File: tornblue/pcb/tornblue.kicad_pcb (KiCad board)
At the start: 2 copper layers, 140.7 x 102.9 mm, 78 parts, among them J1 BATT, J2 SWD, J3 BREAKOUT, J4 USB C - USB2.0, Q1 AO3401A, Q2 AO3401A, SW1 SW_Push, SW10 SW_Push, SW11 SW_Push, SW12 SW_Push, SW13 SW_Push, SW14 SW_Push, SW15 SW_Push, SW16 SW_Push, SW17 SW_Push, SW18 SW_Push, SW19 EC11, SW2 SW_Push, SW20 SW_Push, SW21 SW_Push, SW22 EC11, SW23 RESET, SW3 SW_Push, SW4 SW_Push, SW5 SW_Push, SW6 SW_Push, SW7 SW_Push, SW8 SW_Push, SW9 SW_Push, U1 XC6220, U2 TP4056, U3 nRF52840_holyiot_18010, U4 SRV05-4

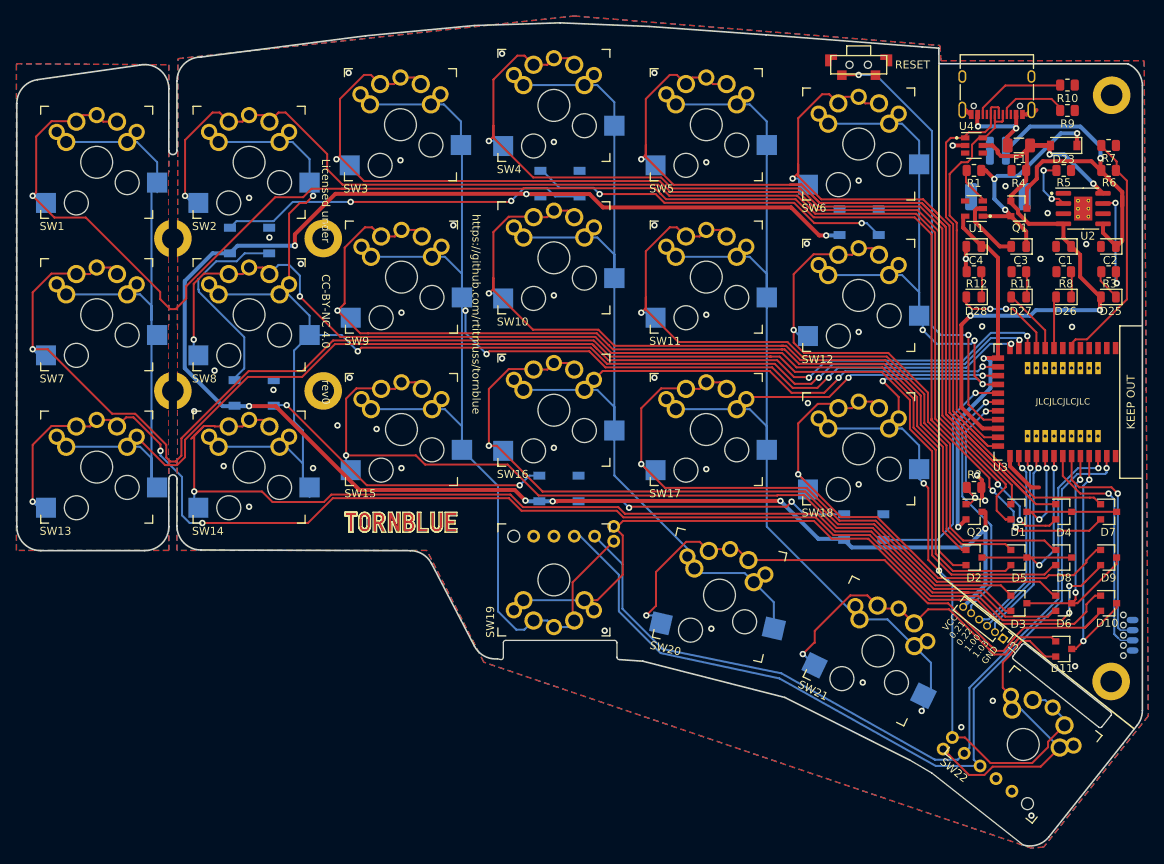
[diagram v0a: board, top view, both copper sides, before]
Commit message: Use m3 mounting holes
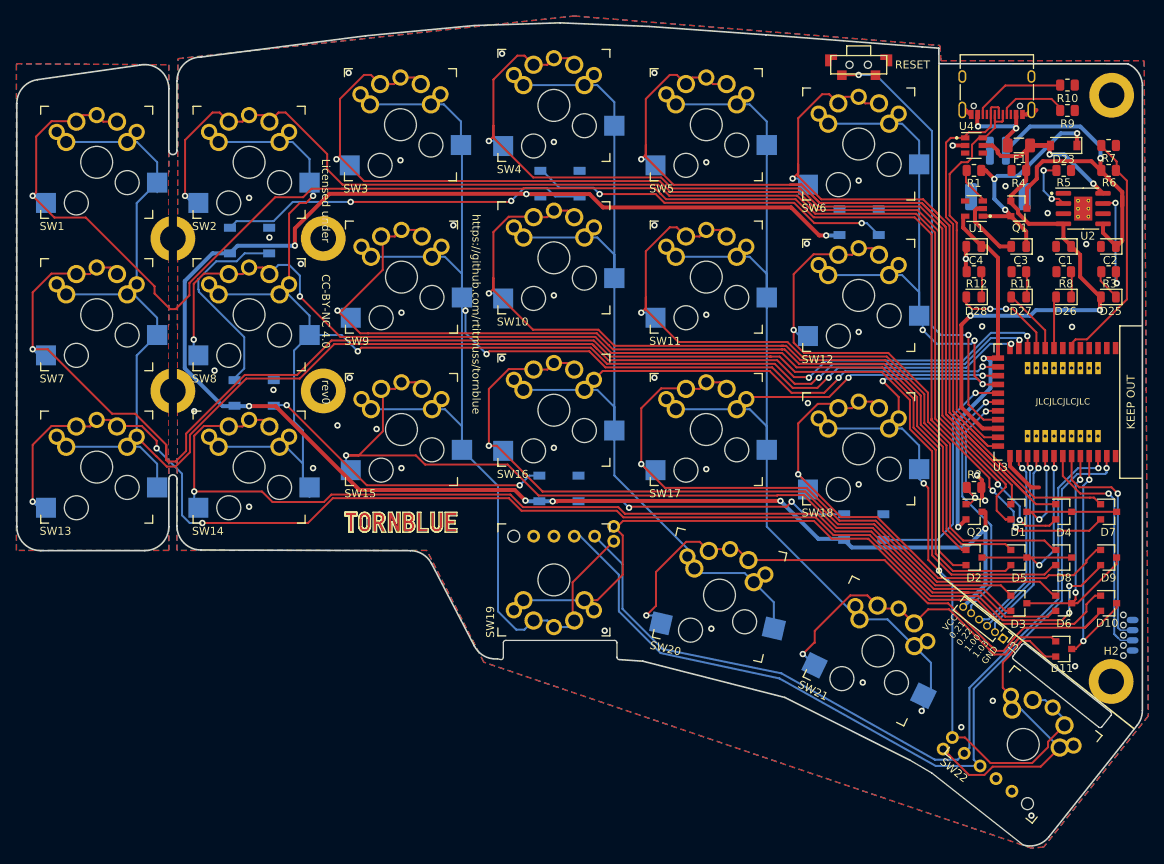
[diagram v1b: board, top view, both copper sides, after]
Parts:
- H1, H2, H3, H4: footprint MountingHole:MountingHole_2.7mm_M2.5_DIN965_Pad -> MountingHole:MountingHole_3.2mm_M3_DIN965_Pad
- H5, H6: footprint tornblue:MountingHole_2.7mm_M2.5_DIN965_Pad_Slot -> tornblue:MountingHole_3.2mm_M3_DIN965_Pad_Slot
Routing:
- net COL0: track 222.2 -> 212.7 mm
- net Net-(D2-Pad2): track 123.8 -> 121.5 mm
- net Net-(D6-Pad2): track 138.4 -> 136.1 mm
- net Net-(D8-Pad2): track 185.7 -> 187.8 mm
- net Net-(D9-Pad2): track 166.3 -> 165.4 mm
- net Net-(D3-Pad2): track 111.4 -> 110.6 mm
- net GND: vias 50 -> 49

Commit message: Smooth board outline
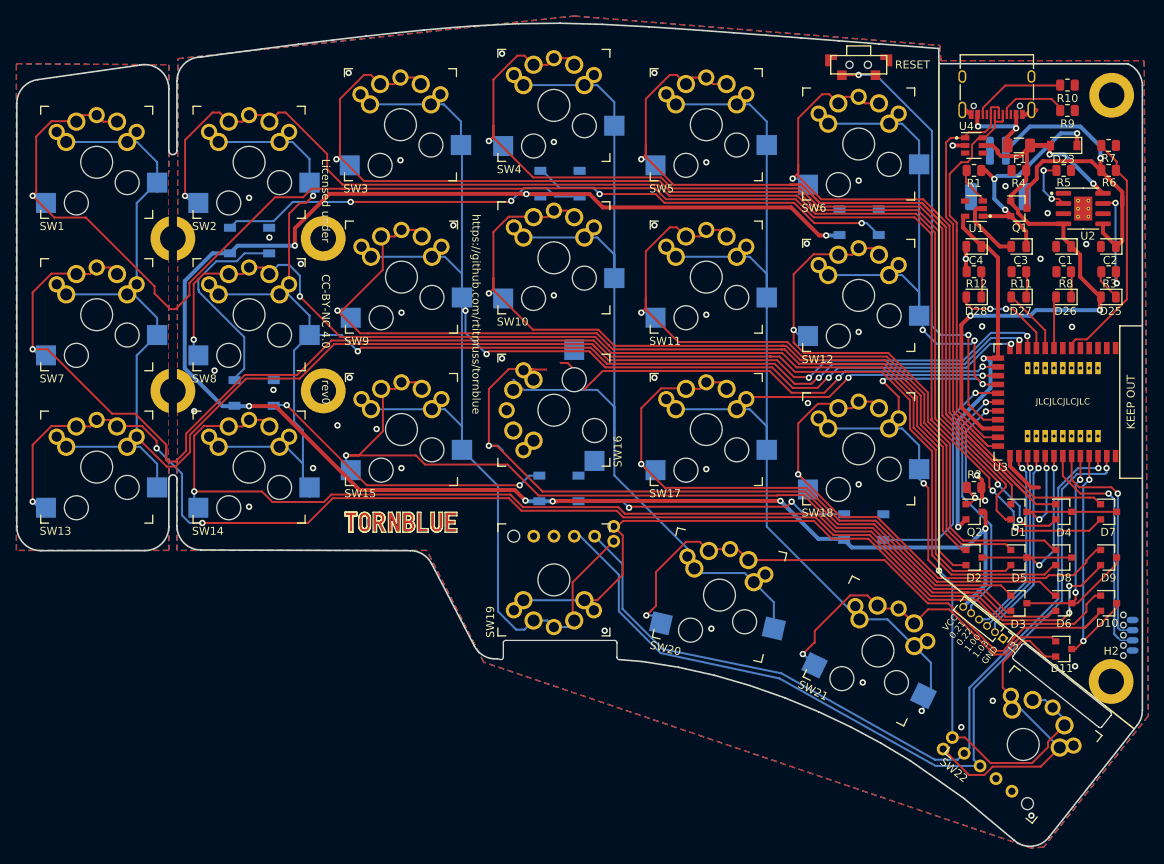
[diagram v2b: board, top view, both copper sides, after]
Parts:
- turned SW16 to 90 degrees
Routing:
- net GND: vias 49 -> 48
- net (no net): vias 0 -> 1
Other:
- outline, holes or cut-outs redrawn

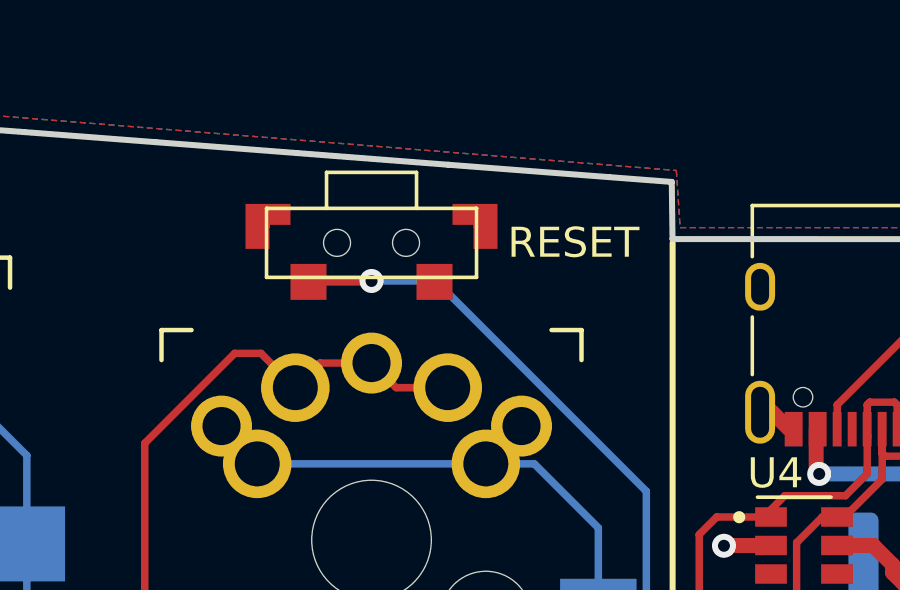
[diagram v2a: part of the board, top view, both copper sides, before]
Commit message: Change to lower profile reset switch
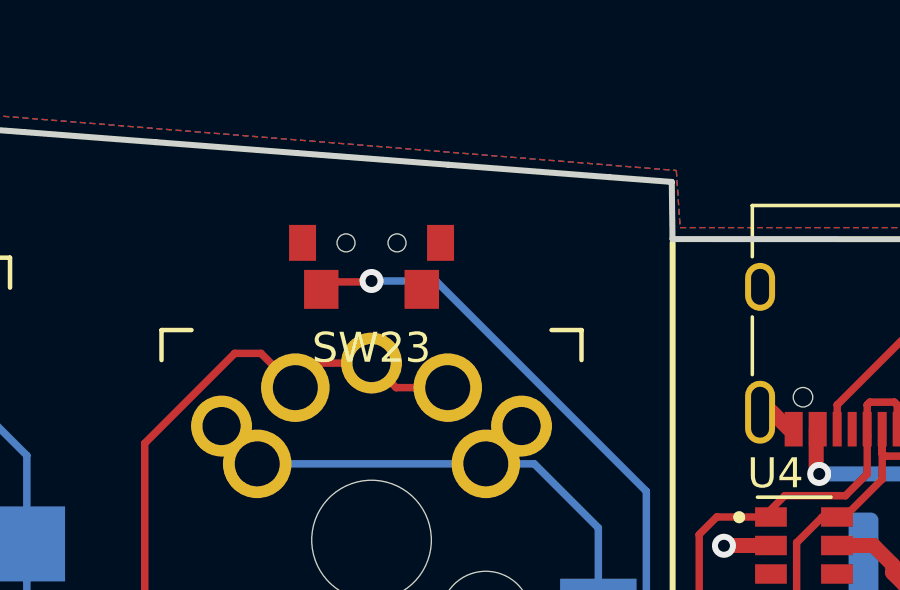
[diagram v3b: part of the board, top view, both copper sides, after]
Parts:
- SW23: footprint tornblue:SW_SPST_TS-1012E-26 -> tornblue:SW_SPST_TS24CA
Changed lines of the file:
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@@
   (layers
     (0 F.Cu signal)
-    (31 B.Cu signal hide)
+    (31 B.Cu signal)
     (32 B.Adhes user hide)
     (33 F.Adhes user hide)
@@
     (add_net "Net-(D13-Pad2)")
     (add_net "Net-(D14-Pad2)")
+    (add_net "Net-(D15-Pad2)")
     (add_net "Net-(D15-Pad4)")
     (add_net "Net-(D16-Pad4)")
@@
     (add_net "Net-(J2-Pad3)")
     (add_net "Net-(J4-PadA5)")
+    (add_net "Net-(J4-PadA8)")
     (add_net "Net-(J4-PadB5)")
+    (add_net "Net-(J4-PadB8)")
     (add_net "Net-(R1-Pad2)")
     (add_net "Net-(R3-Pad2)")
@@
     (add_net "Net-(R6-Pad2)")
     (add_net "Net-(SW23-Pad1)")
+    (add_net "Net-(U1-Pad4)")
+    (add_net "Net-(U2-Pad6)")
+    (add_net "Net-(U3-Pad2)")
+    (add_net "Net-(U3-Pad3)")
+    (add_net "Net-(U3-Pad38)")
+    (add_net "Net-(U3-Pad39)")
+    (add_net "Net-(U3-Pad4)")
+    (add_net "Net-(U3-Pad40)")
+    (add_net "Net-(U3-Pad41)")
+    (add_net "Net-(U3-Pad42)")
+    (add_net "Net-(U3-Pad43)")
+    (add_net "Net-(U3-Pad45)")
+    (add_net "Net-(U3-Pad46)")
+    (add_net "Net-(U3-Pad47)")
+    (add_net "Net-(U3-Pad48)")
+    (add_net "Net-(U3-Pad49)")
+    (add_net "Net-(U3-Pad5)")
+    (add_net "Net-(U3-Pad50)")
+    (add_net "Net-(U3-Pad51)")
+    (add_net "Net-(U3-Pad52)")
+    (add_net "Net-(U3-Pad53)")
+    (add_net "Net-(U3-Pad54)")
+    (add_net "Net-(U3-Pad55)")
+    (add_net "Net-(U3-Pad7)")
+    (add_net "Net-(U4-Pad3)")
+    (add_net "Net-(U4-Pad4)")
     (add_net ROW0)
     (add_net ROW1)
@@
     (add_net VBAT)
     (add_net VBUS)
+  )
+  (module tornblue:SW_SPST_TS24CA locked (layer F.Cu)
+    (at 186.309 52.451)
+    (fp_text reference SW23 (at 0 3.5) (layer F.SilkS)
+      (effects (font (size 1 1) (thickness 0.15)))
+    )
+    (fp_text value RESET (at 0 3.5) (layer F.Fab)
+      (effects (font (size 1 1) (thickness 0.15)))
+    )
+    (fp_line (start -1 -2.1) (end 1 -2.1) (layer F.Fab) (width 0.12))
+    (fp_line (start -2.275 -0.7) (end 2.275 -0.7) (layer F.Fab) (width 0.12))
+    (fp_line (start -2.275 1.6) (end 2.275 1.6) (layer F.Fab) (width 0.12))
+    (fp_line (start -2.275 -0.7) (end -2.275 1.6) (layer F.Fab) (width 0.12))
+    (fp_line (start 2.275 -0.7) (end 2.275 1.6) (layer F.Fab) (width 0.12))
+    (fp_line (start -1 -2.1) (end -1 -0.7) (layer F.Fab) (width 0.12))
+    (fp_line (start 1 -2.1) (end 1 -0.7) (layer F.Fab) (width 0.12))
+    (pad 1 smd rect (at -1.675 1.55) (size 1.15 1.3) (layers F.Cu F.Paste F.Mask)
+      (net 45 "Net-(SW23-Pad1)"))
+    (pad 2 smd rect (at 1.675 1.55) (size 1.15 1.3) (layers F.Cu F.Paste F.Mask)
+      (net 2 GND))
+    (pad "" smd rect (at -2.3 0) (size 0.9 1.2) (layers F.Cu F.Paste F.Mask))
+    (pad "" smd rect (at 2.3 0) (size 0.9 1.2) (layers F.Cu F.Paste F.Mask))
+    (pad "" np_thru_hole circle (at -0.85 0) (size 0.6 0.6) (drill 0.6) (layers *.Cu *.Mask))
+    (pad "" np_thru_hole circle (at 0.85 0) (size 0.6 0.6) (drill 0.6) (layers *.Cu *.Mask))
   )
   (module tornblue:MX_PG1350_EVQWGD001_LR_optional (layer F.Cu)
@@
     )
   )
-  (module tornblue:SW_SPST_TS-1012E-26 locked (layer F.Cu)
-    (at 186.309 52.451)
-    (attr smd)
-    (fp_text reference SW23 (at -0.0127 2.6924) (layer F.SilkS) hide
-      (effects (font (size 1 1) (thickness 0.15)))
-    )
-    (fp_text value RESET (at 6.731 0) (layer F.SilkS)
-      (effects (font (size 1 1) (thickness 0.15)))
-    )
-    (fp_line (start -4.3 2.1) (end -4.3 -1.15) (layer F.CrtYd) (width 0.05))
-    (fp_line (start 4.3 2.1) (end -4.3 2.1) (layer F.CrtYd) (width 0.05))
-    (fp_line (start 4.3 -1.15) (end 4.3 2.1) (layer F.CrtYd) (width 0.05))
-    (fp_line (start -4.3 -1.15) (end 4.3 -1.15) (layer F.CrtYd) (width 0.05))
-    (fp_line (start 1.5 -2.35) (end 1.5 -1.15) (layer F.SilkS) (width 0.12))
-    (fp_line (start -1.5 -2.35) (end -1.5 -1.15) (layer F.SilkS) (width 0.12))
-    (fp_line (start -1.5 -2.35) (end 1.5 -2.35) (layer F.SilkS) (width 0.12))
-    (fp_line (start -3.5 1.15) (end 3.5 1.15) (layer F.SilkS) (width 0.12))
-    (fp_line (start 3.5 -1.15) (end 3.5 1.15) (layer F.SilkS) (width 0.12))
-    (fp_line (start -3.5 -1.15) (end -3.5 1.15) (layer F.SilkS) (width 0.12))
-    (fp_line (start -3.5 -1.15) (end 3.5 -1.15) (layer F.SilkS) (width 0.12))
-    (pad 3 smd custom (at -3.45 -0.55) (size 0.1 0.1) (layers F.Cu F.Paste F.Mask)
-      (zone_connect 0)
-      (options (clearance outline) (anchor rect))
-      (primitives
-        (gr_poly (pts
-           (xy 0.75 -0.75) (xy -0.75 -0.75) (xy -0.75 0.75) (xy 0.05 0.75) (xy 0.05 -0.05)
-           (xy 0.75 -0.05)) (width 0))
-      ))
-    (pad 1 smd rect (at -2.1 1.3) (size 1.2 1.2) (layers F.Cu F.Paste F.Mask)
-      (net 45 "Net-(SW23-Pad1)"))
-    (pad 3 smd custom (at 3.45 -0.55) (size 0.1 0.1) (layers F.Cu F.Paste F.Mask)
-      (zone_connect 0)
-      (options (clearance outline) (anchor rect))
-      (primitives
-        (gr_poly (pts
-           (xy -0.75 -0.75) (xy 0.75 -0.75) (xy 0.75 0.75) (xy -0.05 0.75) (xy -0.05 -0.05)
-           (xy -0.75 -0.05)) (width 0))
-      ))
-    (pad 2 smd rect (at 2.1 1.3) (size 1.2 1.2) (layers F.Cu F.Paste F.Mask)
-      (net 2 GND))
-    (pad "" np_thru_hole circle (at -1.15 0) (size 0.9 0.9) (drill 0.9) (layers *.Cu *.Mask))
-    (pad "" np_thru_hole circle (at 1.15 0) (size 0.9 0.9) (drill 0.9) (layers *.Cu *.Mask))
-  )
   (module Package_TO_SOT_SMD:SOT-23-6 locked (layer F.Cu)

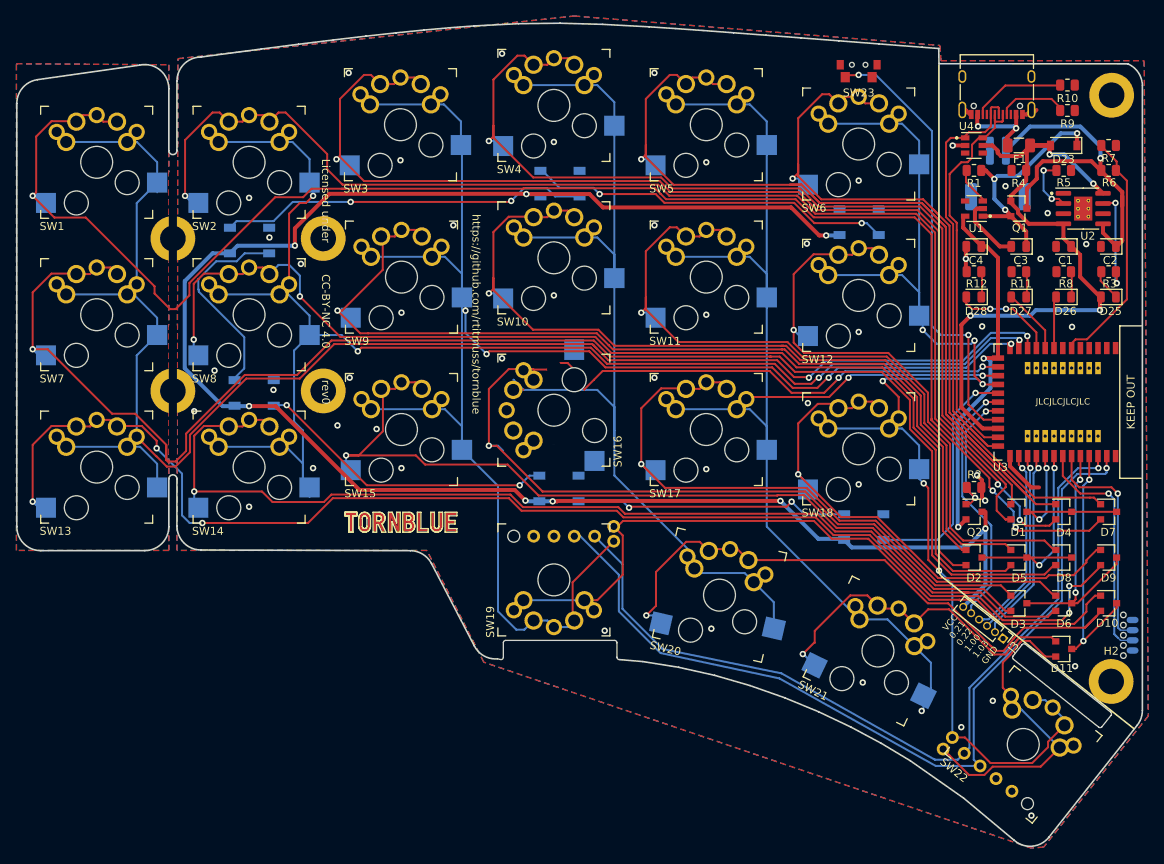
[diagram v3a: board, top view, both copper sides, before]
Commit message: Removed support for Kailh MX sockets
It is not possible to include options for Kailh MX sockets, underglow
LEDS and Panasonic EVQWGD001 encoder on the same PCB.
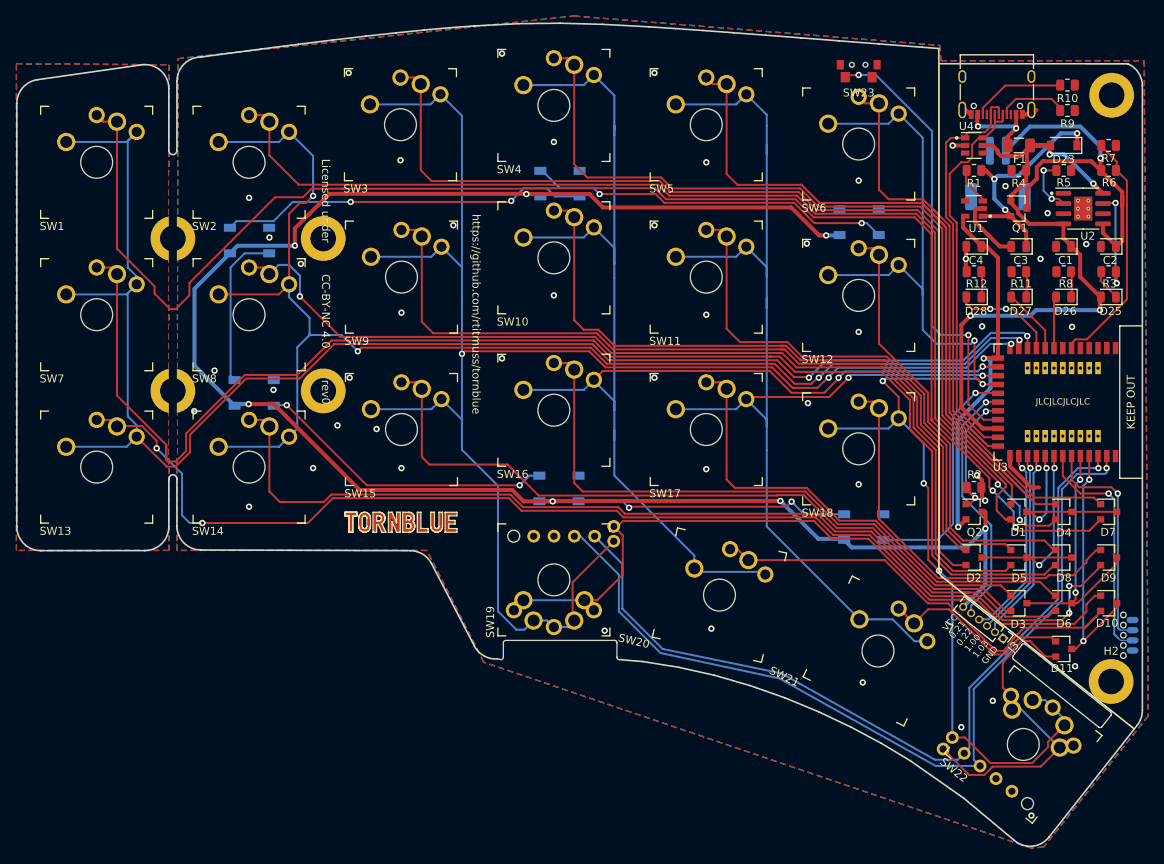
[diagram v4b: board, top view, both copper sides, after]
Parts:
- SW1, SW10, SW11, SW12, SW13, SW14, SW15, SW16, SW17, SW18, SW2, SW20, SW21, SW3, SW4, SW5, SW6, SW7, SW8, SW9: footprint tornblue:Kailh_socket_MX_PG1350_optional_reversible -> tornblue:MX_PG1350_optional
- turned SW16 to 0 degrees
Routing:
- net Net-(D4-Pad1): track 166.7 -> 141.4 mm, vias 1 -> 0
- net COL4: track 178.9 -> 156.5 mm, vias 3 -> 2
- net Net-(D7-Pad1): track 93.6 -> 72.4 mm, vias 1 -> 0
- net Net-(D1-Pad2): track 144.6 -> 123.7 mm, vias 1 -> 0
- net Net-(D5-Pad1): track 90.3 -> 69.7 mm, vias 1 -> 0
- net COL3: track 196.1 -> 176.0 mm
- net Net-(D1-Pad1): track 123.3 -> 103.2 mm, vias 1 -> 0
- net Net-(D8-Pad1): track 74.6 -> 54.8 mm, vias 1 -> 0
- net Net-(D10-Pad2): track 75.8 -> 56.2 mm, vias 1 -> 0
- net COL1: track 187.0 -> 167.9 mm
- net Net-(D2-Pad1): track 104.2 -> 85.2 mm, vias 1 -> 0
- net Net-(D4-Pad2): track 158.6 -> 139.8 mm, vias 3 -> 2
- net Net-(D6-Pad1): track 80.7 -> 62.0 mm, vias 1 -> 0
- net Net-(D6-Pad2): track 136.1 -> 117.5 mm, vias 1 -> 0
- net Net-(D11-Pad1): track 43.5 -> 24.8 mm, vias 1 -> 0
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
